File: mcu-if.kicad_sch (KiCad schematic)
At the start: 50 parts, among them J501 MCU_USB, J502 SD_Card, J503 CONN_DISP, J504 RJ45_Amphenol_RJMG1BD3B8K1ANR, SW501 BTN0, SW502 BTN1, SW503 BTN2, SW504 BTN3, U501 KSZ8081RNA

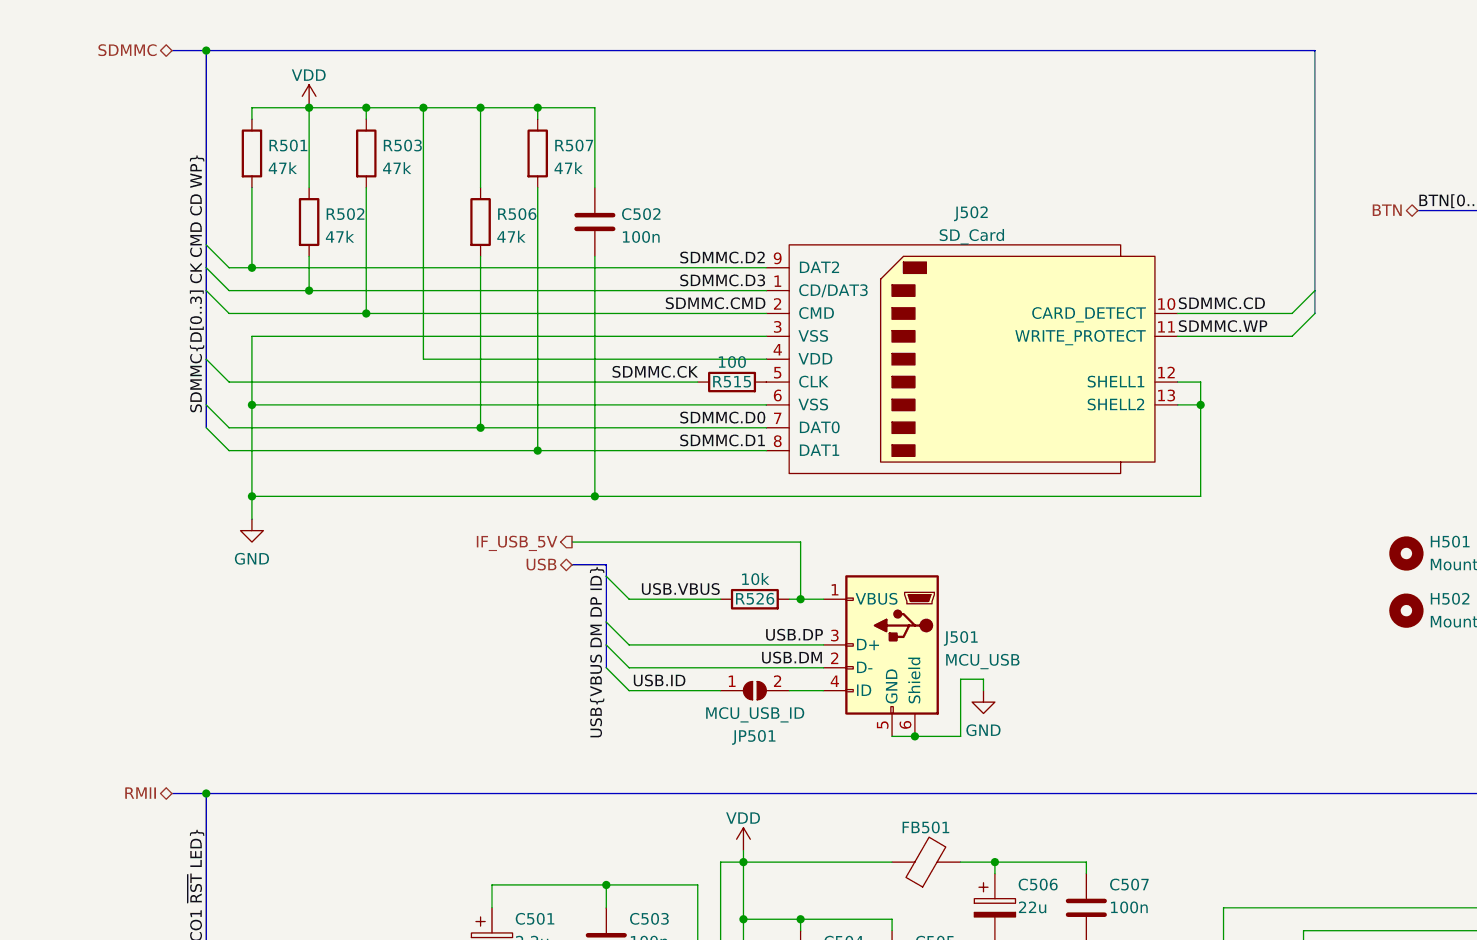
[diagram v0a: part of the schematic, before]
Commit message: Fix several footprints, adjust pcb layout.
- Change footprint for power switch, add the switch's datasheet.
- Rearrange power supply area of PCB to make new switch fit.
- Fix SD card socket footprint to be compatible with the schematic symbol. Add its datasheet
- Add pullups for SD card socket WP and CD (fixed footprint hardwires one side of the switches to GND)
- Add datasheet for the barrel jack.
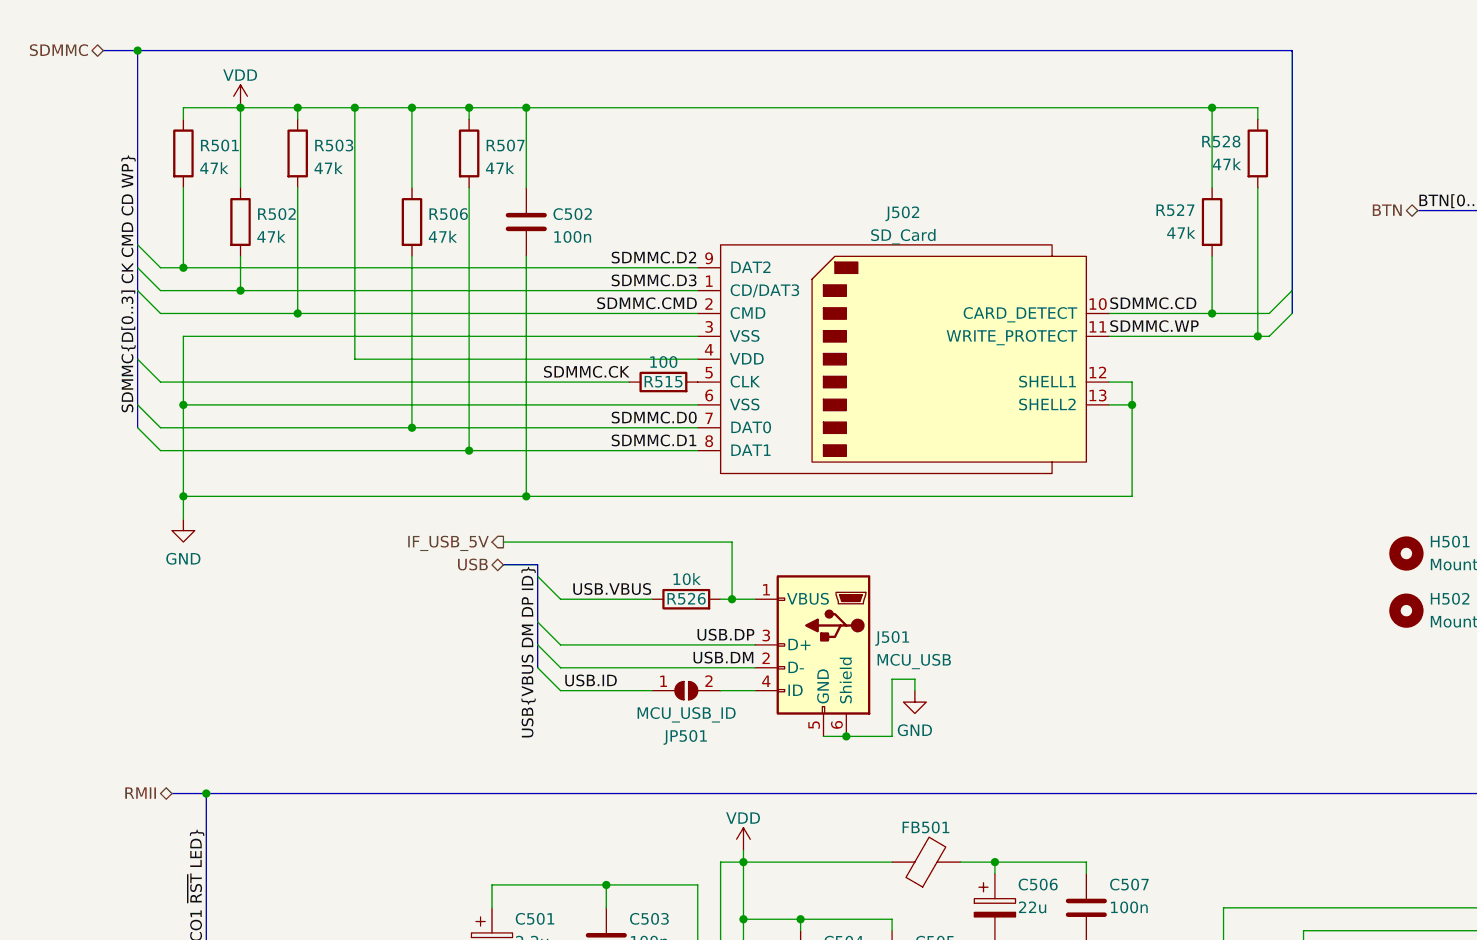
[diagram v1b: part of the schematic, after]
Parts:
- added R527, R528: 47k, Resistor_SMD:R_0603_1608Metric_Pad0.98x0.95mm_HandSolder, symbol Device:R
- J502: footprint Connector_Card:SD_Hirose_DM1AA_SF_PEJ82 -> marco-ram-board:SD_Hirose_DM1AA_SF_PEJ82
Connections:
- net SDMMC.CD: now also R527.2
- net SDMMC.WP: now also R528.2
- net VDD: now also R527.1, R528.1
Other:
- moved on the sheet: C502, J501, J502, JP501, R501, R502, R503, R506, R507, R515, R526

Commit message: Add worksheet template with PoliMi logo.
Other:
- title: (none) -> MARCO RAM Board
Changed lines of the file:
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@@
 (kicad_sch (version 20211123) (generator eeschema)
   (paper "A4")
+  (title_block
+    (title "MARCO RAM Board")
+    (rev "1")
+    (comment 9 "MCU Interfaces")
+  )
   (junction (at 167.64 146.05) (diameter 0) (color 0 0 0 0)
   )

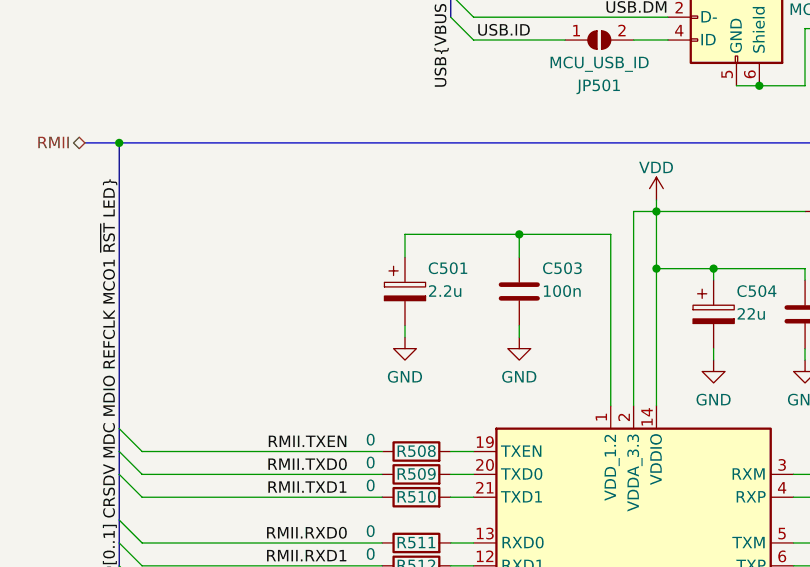
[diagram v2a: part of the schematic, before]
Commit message: Fix C501 symbol, it is a non polarized ceramic
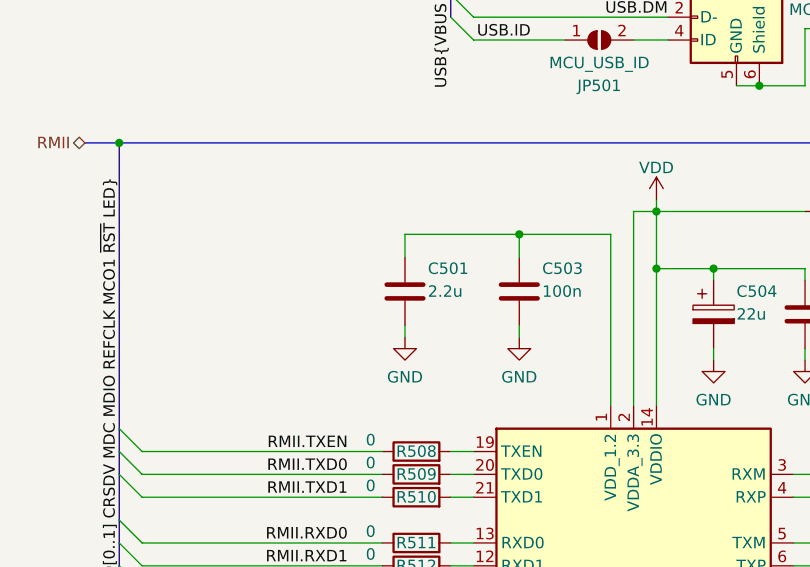
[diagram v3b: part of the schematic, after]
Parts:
- C501: symbol Device:C_Polarized -> Device:C
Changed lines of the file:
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@@
     (pin "2")
   )
-  (symbol (lib_id "Device:C_Polarized") (at 72.39 118.11 0) (unit 1)
+  (symbol (lib_id "Device:C") (at 72.39 118.11 0) (unit 1)
     (in_bom yes) (on_board yes)
     (property "Reference" "C501" (id 0) (at 74.93 115.57 0)

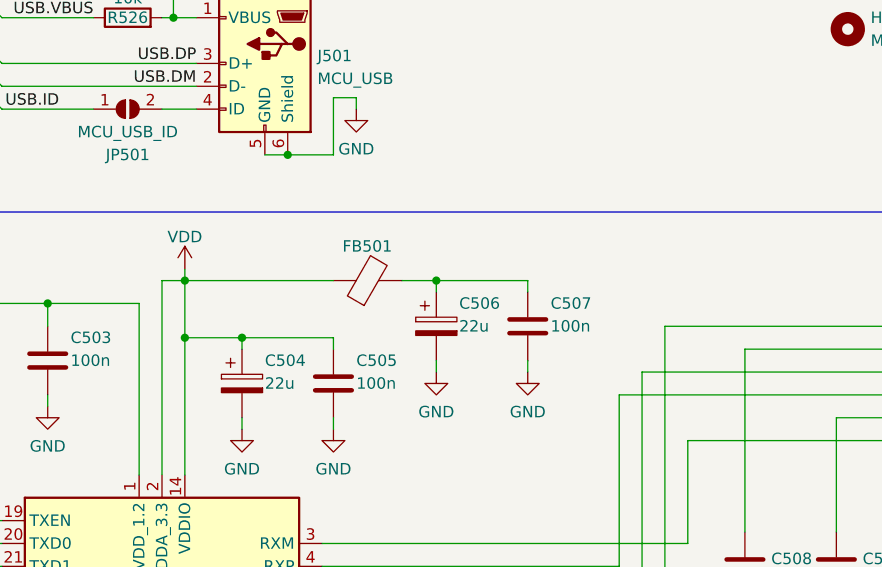
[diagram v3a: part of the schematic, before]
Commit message: Fix ferrite bead from the wrong side
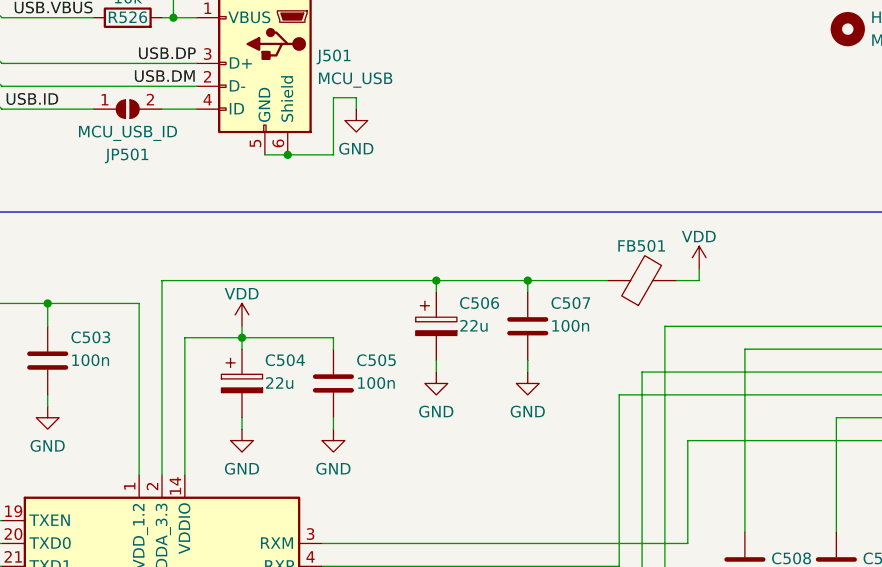
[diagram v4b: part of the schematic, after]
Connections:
- net VDD: now also FB501.2; no longer FB501.1, U501.2 (VDDA_3.3)
- net at C506.1, C507.1: now also FB501.1, U501.2 (VDDA_3.3); no longer FB501.2
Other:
- moved on the sheet: FB501
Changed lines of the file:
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@@
   (junction (at 205.74 88.9) (diameter 0) (color 0 0 0 0)
   )
-  (junction (at 100.33 109.22) (diameter 0) (color 0 0 0 0)
+  (junction (at 138.43 109.22) (diameter 0) (color 0 0 0 0)
   )
   (junction (at 207.01 20.32) (diameter 0) (color 0 0 0 0)
@@
   )
   (junction (at 99.06 80.01) (diameter 0) (color 0 0 0 0)
-  )
-  (junction (at 100.33 115.57) (diameter 0) (color 0 0 0 0)
   )
   (junction (at 251.46 49.53) (diameter 0) (color 0 0 0 0)
@@
     (stroke (width 0) (type default) (color 0 0 0 0))
   )
-  (wire (pts (xy 97.79 109.22) (xy 100.33 109.22))
+  (wire (pts (xy 97.79 109.22) (xy 128.27 109.22))
     (stroke (width 0) (type default) (color 0 0 0 0))
   )
@@
     (stroke (width 0) (type default) (color 0 0 0 0))
   )
-  (wire (pts (xy 124.46 109.22) (xy 128.27 109.22))
-    (stroke (width 0) (type default) (color 0 0 0 0))
-  )
   (wire (pts (xy 35.56 63.5) (xy 69.85 63.5))
     (stroke (width 0) (type default) (color 0 0 0 0))
@@
     (stroke (width 0) (type default) (color 0 0 0 0))
   )
+  (wire (pts (xy 157.48 109.22) (xy 157.48 107.95))
+    (stroke (width 0) (type default) (color 0 0 0 0))
+  )
   (wire (pts (xy 69.85 25.4) (xy 76.2 25.4))
     (stroke (width 0) (type default) (color 0 0 0 0))
@@
     (stroke (width 0) (type default) (color 0 0 0 0))
   )
+  (wire (pts (xy 106.68 114.3) (xy 106.68 115.57))
+    (stroke (width 0) (type default) (color 0 0 0 0))
+  )
   (wire (pts (xy 185.42 163.83) (xy 193.04 163.83))
     (stroke (width 0) (type default) (color 0 0 0 0))
@@
     (stroke (width 0) (type default) (color 0 0 0 0))
   )
-  (wire (pts (xy 100.33 115.57) (xy 100.33 109.22))
-    (stroke (width 0) (type default) (color 0 0 0 0))
-  )
   (wire (pts (xy 35.56 45.72) (xy 44.45 45.72))
     (stroke (width 0) (type default) (color 0 0 0 0))
@@
     (stroke (width 0) (type default) (color 0 0 0 0))
   )
+  (wire (pts (xy 154.94 109.22) (xy 157.48 109.22))
+    (stroke (width 0) (type default) (color 0 0 0 0))
+  )
   (wire (pts (xy 152.4 41.91) (xy 152.4 48.26))
     (stroke (width 0) (type default) (color 0 0 0 0))
@@
     (stroke (width 0) (type default) (color 0 0 0 0))
   )
-  (wire (pts (xy 100.33 109.22) (xy 116.84 109.22))
-    (stroke (width 0) (type default) (color 0 0 0 0))
-  )
   (wire (pts (xy 234.95 76.2) (xy 250.19 76.2))
     (stroke (width 0) (type default) (color 0 0 0 0))
@@
     (stroke (width 0) (type default) (color 0 0 0 0))
   )
-  (wire (pts (xy 100.33 107.95) (xy 100.33 109.22))
-    (stroke (width 0) (type default) (color 0 0 0 0))
-  )
   (wire (pts (xy 251.46 137.16) (xy 251.46 146.05))
     (stroke (width 0) (type default) (color 0 0 0 0))
@@
   )
   (wire (pts (xy 215.9 20.32) (xy 215.9 22.86))
+    (stroke (width 0) (type default) (color 0 0 0 0))
+  )
+  (wire (pts (xy 138.43 109.22) (xy 147.32 109.22))
     (stroke (width 0) (type default) (color 0 0 0 0))
   )
@@
     (pin "2")
   )
-  (symbol (lib_id "power:VDD") (at 100.33 107.95 0) (unit 1)
-    (in_bom yes) (on_board yes) (fields_autoplaced)
-    (property "Reference" "#PWR0507" (id 0) (at 100.33 111.76 0)
-      (effects (font (size 1.27 1.27)) hide)
-    )
-    (property "Value" "VDD" (id 1) (at 100.33 104.3742 0))
-    (property "Footprint" "" (id 2) (at 100.33 107.95 0)
-      (effects (font (size 1.27 1.27)) hide)
-    )
-    (property "Datasheet" "" (id 3) (at 100.33 107.95 0)
+  (symbol (lib_id "power:VDD") (at 157.48 107.95 0) (unit 1)
+    (in_bom yes) (on_board yes)
+    (property "Reference" "#PWR0507" (id 0) (at 157.48 111.76 0)
+      (effects (font (size 1.27 1.27)) hide)
+    )
+    (property "Value" "VDD" (id 1) (at 157.48 104.3742 0))
+    (property "Footprint" "" (id 2) (at 157.48 107.95 0)
+      (effects (font (size 1.27 1.27)) hide)
+    )
+    (property "Datasheet" "" (id 3) (at 157.48 107.95 0)
       (effects (font (size 1.27 1.27)) hide)
     )
@@
     (pin "1")
   )
-  (symbol (lib_id "Device:FerriteBead") (at 120.65 109.22 90) (unit 1)
-    (in_bom yes) (on_board yes) (fields_autoplaced)
-    (property "Reference" "FB501" (id 0) (at 120.5992 105.4156 90))
-    (property "Value" "FerriteBead" (id 1) (at 120.5992 105.4155 90)
-      (effects (font (size 1.27 1.27)) hide)
-    )
-    (property "Footprint" "Inductor_SMD:L_0603_1608Metric_Pad1.05x0.95mm_HandSolder" (id 2) (at 120.65 110.998 90)
-      (effects (font (size 1.27 1.27)) hide)
-    )
-    (property "Datasheet" "~" (id 3) (at 120.65 109.22 0)
-      (effects (font (size 1.27 1.27)) hide)
-    )
-    (property "Part" "815-ACML-0603H-301" (id 4) (at 120.65 109.22 90)
+  (symbol (lib_id "Device:FerriteBead") (at 151.13 109.22 90) (unit 1)
+    (in_bom yes) (on_board yes) (fields_autoplaced)
+    (property "Reference" "FB501" (id 0) (at 151.0792 105.4156 90))
+    (property "Value" "FerriteBead" (id 1) (at 151.0792 105.4155 90)
+      (effects (font (size 1.27 1.27)) hide)
+    )
+    (property "Footprint" "Inductor_SMD:L_0603_1608Metric_Pad1.05x0.95mm_HandSolder" (id 2) (at 151.13 110.998 90)
+      (effects (font (size 1.27 1.27)) hide)
+    )
+    (property "Datasheet" "~" (id 3) (at 151.13 109.22 0)
+      (effects (font (size 1.27 1.27)) hide)
+    )
+    (property "Part" "815-ACML-0603H-301" (id 4) (at 151.13 109.22 90)
       (effects (font (size 1.27 1.27)) hide)
     )
@@
     (pin "2")
   )
+  (symbol (lib_id "power:VDD") (at 106.68 114.3 0) (unit 1)
+    (in_bom yes) (on_board yes) (fields_autoplaced)
+    (property "Reference" "#PWR0101" (id 0) (at 106.68 118.11 0)
+      (effects (font (size 1.27 1.27)) hide)
+    )
+    (property "Value" "VDD" (id 1) (at 106.68 110.7242 0))
+    (property "Footprint" "" (id 2) (at 106.68 114.3 0)
+      (effects (font (size 1.27 1.27)) hide)
+    )
+    (property "Datasheet" "" (id 3) (at 106.68 114.3 0)
+      (effects (font (size 1.27 1.27)) hide)
+    )
+    (pin "1")
+  )
   (symbol (lib_id "Device:R") (at 185.42 144.78 0) (unit 1)

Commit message: BON consolidation
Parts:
- R505, R515: value 100 -> 220
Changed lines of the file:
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@@
     (in_bom yes) (on_board yes)
     (property "Reference" "R515" (id 0) (at 91.44 55.88 90))
-    (property "Value" "100" (id 1) (at 91.44 53.7011 90))
+    (property "Value" "220" (id 1) (at 91.44 53.7011 90))
     (property "Footprint" "Resistor_SMD:R_0603_1608Metric_Pad0.98x0.95mm_HandSolder" (id 2) (at 91.44 57.658 90)
       (effects (font (size 1.27 1.27)) hide)
@@
     (in_bom yes) (on_board yes)
     (property "Reference" "R505" (id 0) (at 63.5 179.07 90))
-    (property "Value" "100" (id 1) (at 63.5 176.8911 90))
+    (property "Value" "220" (id 1) (at 63.5 176.8911 90))
     (property "Footprint" "Resistor_SMD:R_0603_1608Metric_Pad0.98x0.95mm_HandSolder" (id 2) (at 63.5 180.848 90)
       (effects (font (size 1.27 1.27)) hide)

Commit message: BOM consolidations
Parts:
- R525: value 1.5k -> 1k
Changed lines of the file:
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@@
   (symbol (lib_id "Device:R") (at 260.35 43.18 0) (unit 1)
     (in_bom yes) (on_board yes) (fields_autoplaced)
-    (property "Reference" "R525" (id 0) (at 262.128 42.3453 0)
+    (property "Reference" "R525" (id 0) (at 262.89 41.9099 0)
       (effects (font (size 1.27 1.27)) (justify left))
     )
-    (property "Value" "1.5k" (id 1) (at 262.128 44.8822 0)
+    (property "Value" "1k" (id 1) (at 262.89 44.4499 0)
       (effects (font (size 1.27 1.27)) (justify left))
     )

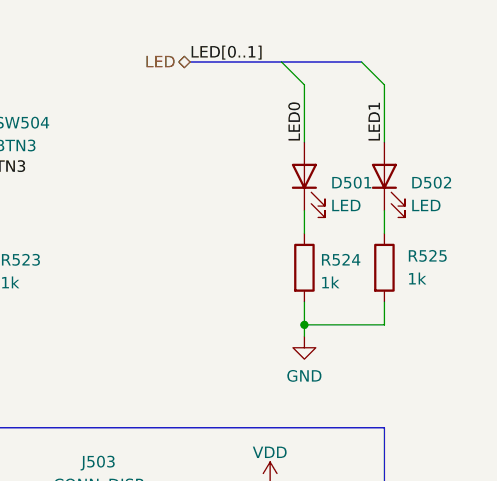
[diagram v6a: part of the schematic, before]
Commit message: Fully update PCB and schematic after BOM consolidation
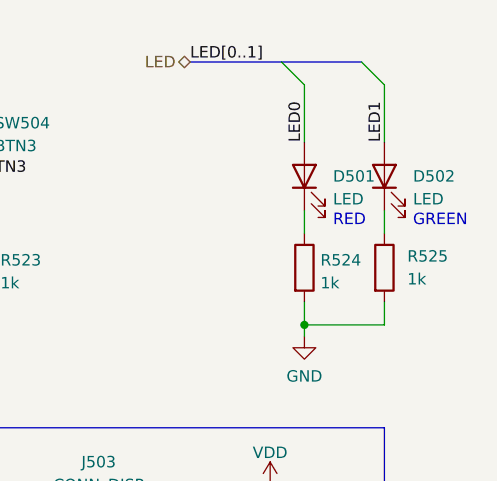
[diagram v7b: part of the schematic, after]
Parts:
- C501: Part (none) -> 187-CL10A225KQ8NNNC
- C502, C503, C505, C507, C508, C509: Part (none) -> 603-CC603ZRY5V7BB104
- C504, C506: Part 74-293D226X96R3A2TE3 -> 581-TPSA226M006R0500
- D501: Part (none) -> 720-LST676-R1S1-1-Z
- D502: Part (none) -> 327-VCEG1104LSTR
- FB501: Part 815-ACML-0603H-301 -> 603-PBY160808T-301YN
- H501, H502: now left out of the parts list
- J501: Part (none) -> 710-65100516121
- J502: Part (none) -> 798-DM1AA-SF-PEJ82
- J504: Part (none) -> 523-RJMG1BD3B8K1ANR
- R501, R502, R503, R506, R507, R527, R528: Part (none) -> 791-RMC1/16K4702FTP
- R504, R526: Part (none) -> 791-RMC1/16-1002FTP
- R505, R515, R518, R521: Part (none) -> 791-RMC1/16-221JTP
- R508, R509, R510, R511, R512, R513, R514: Part (none) -> 652-CR0603-J/-000ELF
- R516: Part (none) -> 652-CR0603FX-6491ELF
- R517, R520, R522, R523, R524, R525: Part (none) -> 603-RC0603FR-071KL
- R519: Part (none) -> 791-RMC1/16-472JTP
- SW501, SW502, SW503, SW504: Part (none) -> 113-DTSMW-69N-V-T/R
- U501: Part (none) -> 998-KSZ8081RNACA
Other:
- note added: "GREEN"
- note added: "RED"
